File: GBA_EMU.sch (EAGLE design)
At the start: 98 parts, among them J1 USB-MINIB-5PIN, J2 AVR_SPI, SW1 LEFT, SW2 RIGHT, SW3 PWR_SWITCH, U1 MIC7221, U2 MCP1642B-ADJ, U4 LM4875, U5 Mic5365-2.8Y, U7 AZV321, X2 HEADPHONE

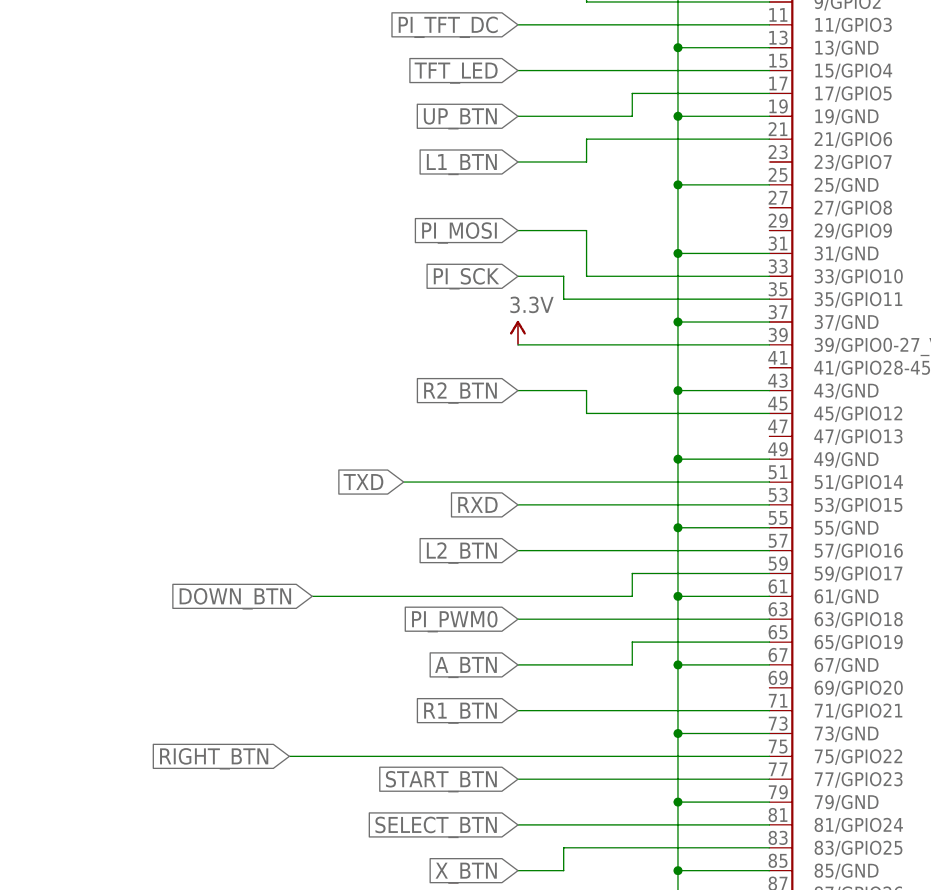
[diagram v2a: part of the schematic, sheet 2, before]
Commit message: moved connectors and whatnot
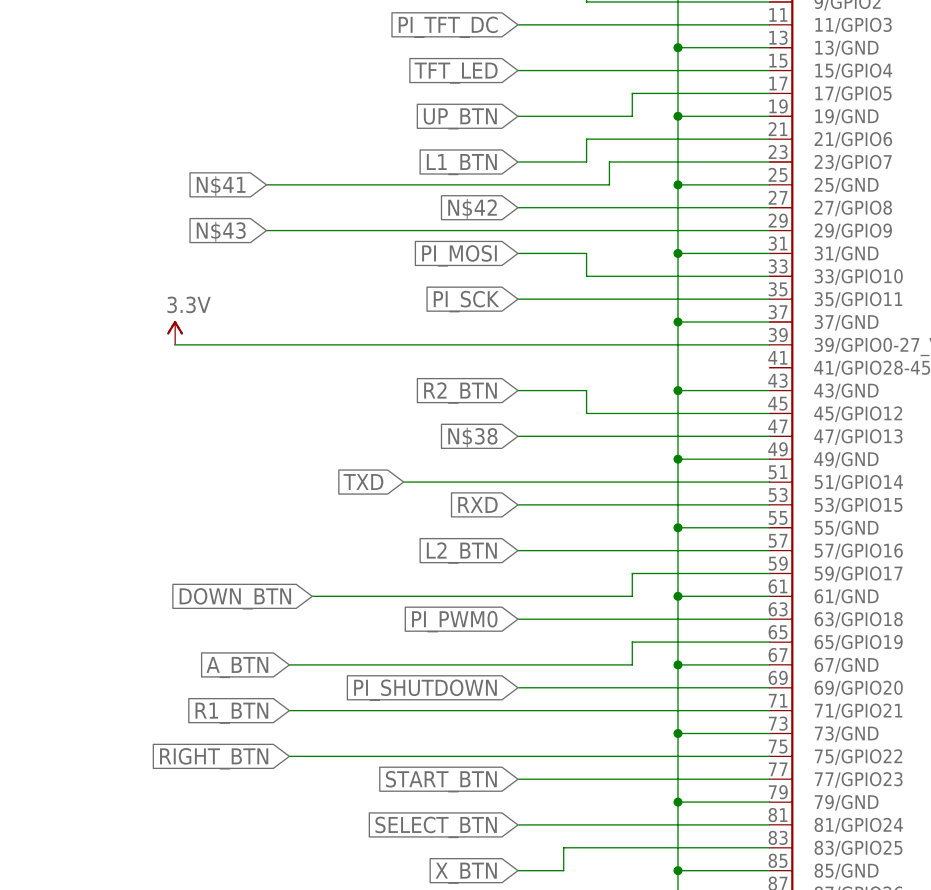
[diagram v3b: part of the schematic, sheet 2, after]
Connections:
- new net N$38: PCB1.47/GPIO13
- new net N$41: PCB1.23/GPIO7
- new net N$42: PCB1.27/GPIO8
- new net N$43: PCB1.29/GPIO9
- new net PI_SHUTDOWN: PCB1.69/GPIO20
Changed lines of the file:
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@@
 <instance part="FRAME2" gate="G$1" x="-106.68" y="-104.14"/>
 <instance part="FRAME2" gate="G$2" x="223.52" y="-104.14"/>
-<instance part="SUPPLY5" gate="G$1" x="10.16" y="106.68"/>
+<instance part="SUPPLY5" gate="G$1" x="-27.94" y="106.68"/>
 <instance part="SUPPLY11" gate="G$1" x="167.64" y="165.1"/>
 <instance part="GND13" gate="1" x="167.64" y="137.16"/>
@@
 <pinref part="SUPPLY5" gate="G$1" pin="3.3V"/>
 <pinref part="PCB1" gate="G$1" pin="39/GPIO0-27_VREF"/>
-<wire x1="10.16" y1="106.68" x2="38.1" y2="106.68" width="0.1524" layer="91"/>
+<wire x1="-27.94" y1="106.68" x2="38.1" y2="106.68" width="0.1524" layer="91"/>
 </segment>
 <segment>
@@
 <wire x1="38.1" y1="73.66" x2="22.86" y2="73.66" width="0.1524" layer="91"/>
 <wire x1="22.86" y1="73.66" x2="22.86" y2="71.12" width="0.1524" layer="91"/>
-<wire x1="22.86" y1="71.12" x2="10.16" y2="71.12" width="0.1524" layer="91"/>
-<label x="10.16" y="71.12" size="1.778" layer="95" rot="R180" xref="yes"/>
+<wire x1="22.86" y1="71.12" x2="-15.24" y2="71.12" width="0.1524" layer="91"/>
+<label x="-15.24" y="71.12" size="1.778" layer="95" rot="R180" xref="yes"/>
 </segment>
 </net>
@@
 <pinref part="PCB1" gate="G$1" pin="33/GPIO10"/>
 <wire x1="38.1" y1="114.3" x2="17.78" y2="114.3" width="0.1524" layer="91"/>
-<wire x1="17.78" y1="114.3" x2="17.78" y2="119.38" width="0.1524" layer="91"/>
-<wire x1="17.78" y1="119.38" x2="10.16" y2="119.38" width="0.1524" layer="91"/>
-<label x="10.16" y="119.38" size="1.778" layer="95" rot="R180" xref="yes"/>
+<wire x1="17.78" y1="114.3" x2="17.78" y2="116.84" width="0.1524" layer="91"/>
+<wire x1="17.78" y1="116.84" x2="10.16" y2="116.84" width="0.1524" layer="91"/>
+<label x="10.16" y="116.84" size="1.778" layer="95" rot="R180" xref="yes"/>
 </segment>
 </net>
@@
 <segment>
 <pinref part="PCB1" gate="G$1" pin="35/GPIO11"/>
-<wire x1="38.1" y1="111.76" x2="15.24" y2="111.76" width="0.1524" layer="91"/>
-<wire x1="15.24" y1="111.76" x2="15.24" y2="114.3" width="0.1524" layer="91"/>
-<wire x1="15.24" y1="114.3" x2="10.16" y2="114.3" width="0.1524" layer="91"/>
-<label x="10.16" y="114.3" size="1.778" layer="95" rot="R180" xref="yes"/>
+<wire x1="38.1" y1="111.76" x2="10.16" y2="111.76" width="0.1524" layer="91"/>
+<label x="10.16" y="111.76" size="1.778" layer="95" rot="R180" xref="yes"/>
 </segment>
 </net>
@@
 <segment>
 <pinref part="PCB1" gate="G$1" pin="71/GPIO21"/>
-<wire x1="38.1" y1="66.04" x2="10.16" y2="66.04" width="0.1524" layer="91"/>
-<label x="10.16" y="66.04" size="1.778" layer="95" rot="R180" xref="yes"/>
+<wire x1="38.1" y1="66.04" x2="-15.24" y2="66.04" width="0.1524" layer="91"/>
+<label x="-15.24" y="66.04" size="1.778" layer="95" rot="R180" xref="yes"/>
 </segment>
 </net>
@@
 </segment>
 </net>
+<net name="PI_SHUTDOWN" class="0">
+<segment>
+<pinref part="PCB1" gate="G$1" pin="69/GPIO20"/>
+<wire x1="38.1" y1="68.58" x2="10.16" y2="68.58" width="0.1524" layer="91"/>
+<label x="10.16" y="68.58" size="1.778" layer="95" rot="R180" xref="yes"/>
+</segment>
+</net>
+<net name="N$38" class="0">
+<segment>
+<pinref part="PCB1" gate="G$1" pin="47/GPIO13"/>
+<wire x1="38.1" y1="96.52" x2="10.16" y2="96.52" width="0.1524" layer="91"/>
+<label x="10.16" y="96.52" size="1.778" layer="95" rot="R180" xref="yes"/>
+</segment>
+</net>
+<net name="N$41" class="0">
+<segment>
+<pinref part="PCB1" gate="G$1" pin="23/GPIO7"/>
+<wire x1="38.1" y1="127" x2="20.32" y2="127" width="0.1524" layer="91"/>
+<wire x1="20.32" y1="127" x2="20.32" y2="124.46" width="0.1524" layer="91"/>
+<wire x1="20.32" y1="124.46" x2="-17.78" y2="124.46" width="0.1524" layer="91"/>
+<label x="-17.78" y="124.46" size="1.778" layer="95" rot="R180" xref="yes"/>
+</segment>
+</net>
+<net name="N$42" class="0">
+<segment>
+<pinref part="PCB1" gate="G$1" pin="27/GPIO8"/>
+<wire x1="38.1" y1="121.92" x2="10.16" y2="121.92" width="0.1524" layer="91"/>
+<label x="10.16" y="121.92" size="1.778" layer="95" rot="R180" xref="yes"/>
+</segment>
+</net>
+<net name="N$43" class="0">
+<segment>
+<pinref part="PCB1" gate="G$1" pin="29/GPIO9"/>
+<wire x1="38.1" y1="119.38" x2="-17.78" y2="119.38" width="0.1524" layer="91"/>
+<label x="-17.78" y="119.38" size="1.778" layer="95" rot="R180" xref="yes"/>
+</segment>
+</net>

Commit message: updated board render
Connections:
- removed net N$38: PCB1.47/GPIO13
- net Y_BTN: now also PCB1.47/GPIO13
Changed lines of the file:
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@@
 </segment>
 </net>
-<net name="N$38" class="0">
+<net name="Y_BTN" class="0">
 <segment>
 <pinref part="PCB1" gate="G$1" pin="47/GPIO13"/>

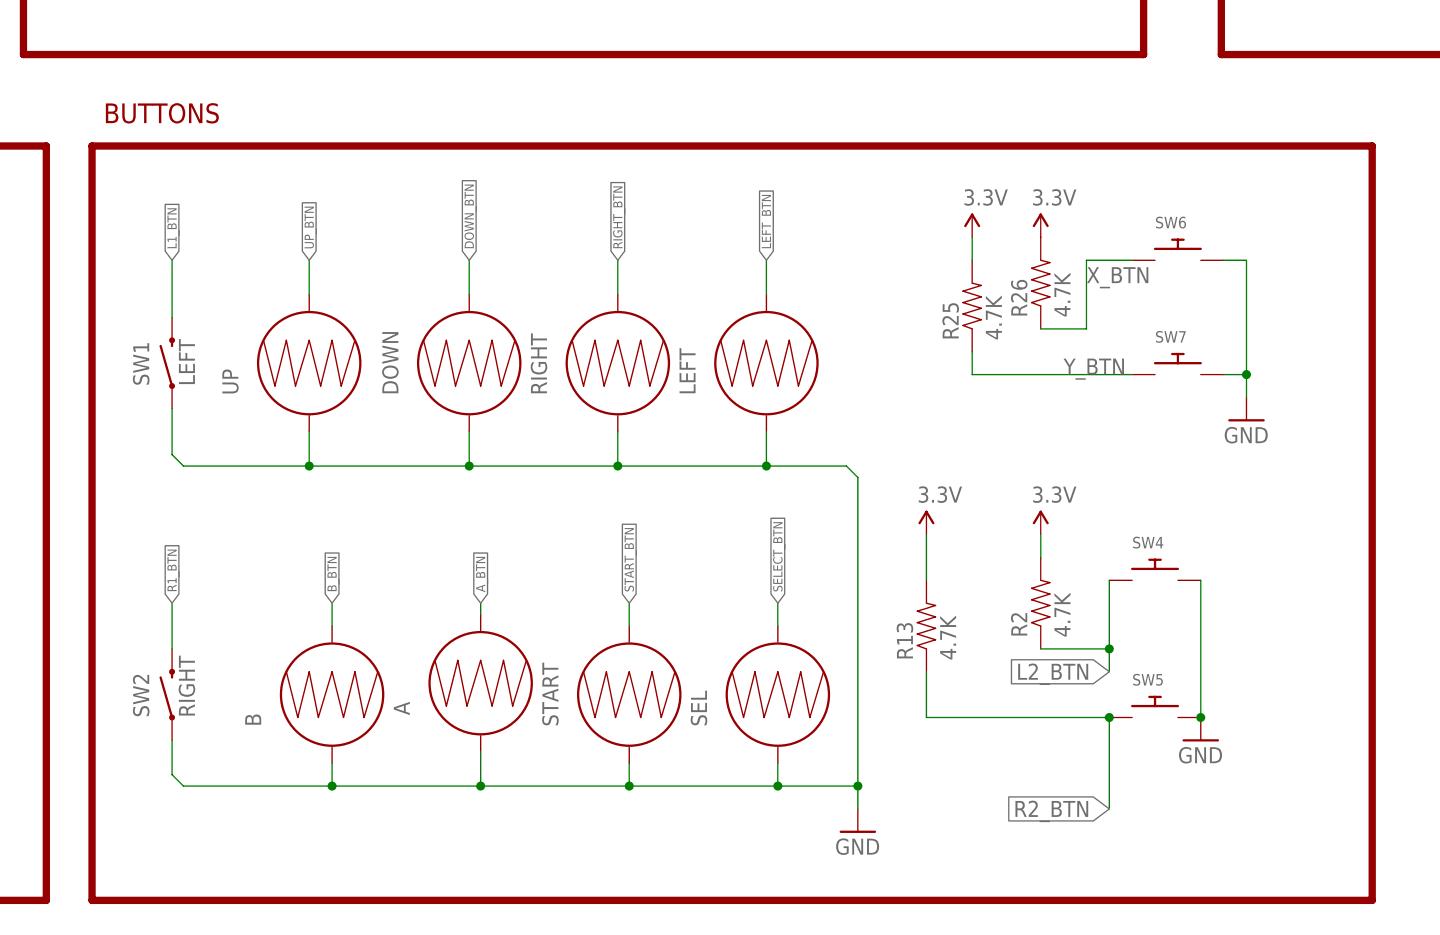
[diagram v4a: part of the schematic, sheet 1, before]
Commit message: moved some labels around
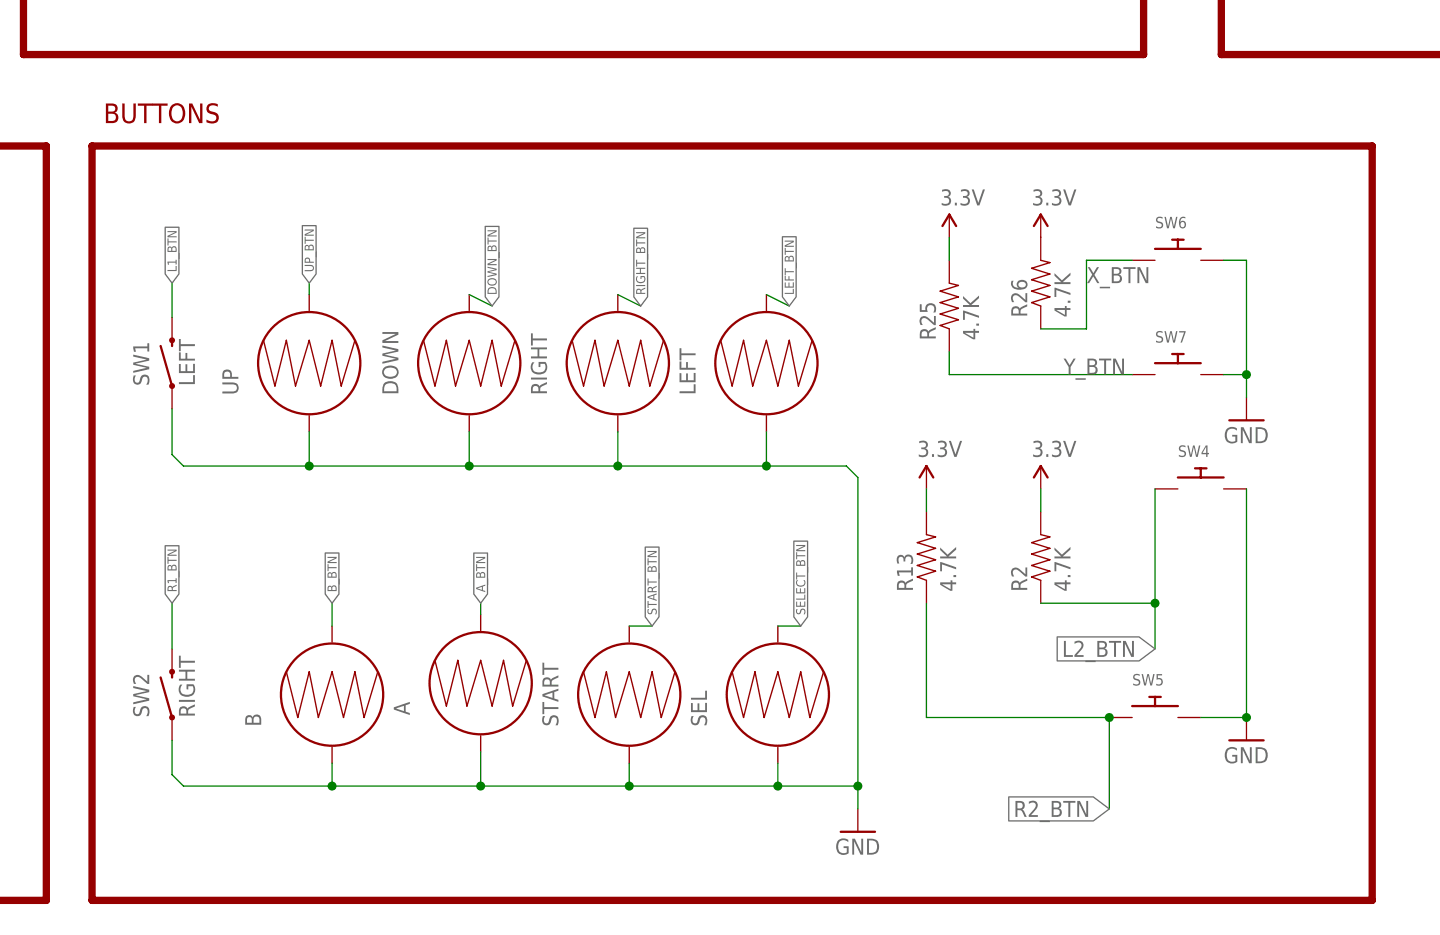
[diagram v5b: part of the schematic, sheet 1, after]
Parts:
- added R24: 10K, SparkFun-Resistors:10KOHM-1/10W-1%(0603)0603
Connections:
- new net N$38: R24.2
- net PWR_EN: now also R24.1
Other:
- moved on the sheet: R13, R2, R25, SW4
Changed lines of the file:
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@@
 <part name="SUPPLY34" library="SparkFun-Aesthetics" deviceset="3.3V" device=""/>
 <part name="SUPPLY38" library="SparkFun-Aesthetics" deviceset="1.8V" device=""/>
+<part name="R24" library="SparkFun-Resistors" deviceset="10KOHM-1/10W-1%(0603)" device="0603" value="10K"/>
 </parts>
 <sheets>
@@
 <instance part="U$1" gate="G$1" x="238.76" y="12.7"/>
 <instance part="POT1" gate="SW" x="304.8" y="152.4" rot="R90"/>
-<instance part="SW4" gate="G$1" x="426.72" y="2.54"/>
+<instance part="SW4" gate="G$1" x="431.8" y="12.7"/>
 <instance part="SW5" gate="G$1" x="426.72" y="-12.7"/>
-<instance part="GND16" gate="1" x="431.8" y="-15.24"/>
-<instance part="SUPPLY9" gate="G$1" x="401.32" y="7.62"/>
-<instance part="R13" gate="G$1" x="401.32" y="-2.54" rot="R90"/>
+<instance part="GND16" gate="1" x="436.88" y="-15.24"/>
+<instance part="SUPPLY9" gate="G$1" x="401.32" y="12.7"/>
+<instance part="R13" gate="G$1" x="401.32" y="5.08" rot="R90"/>
 <instance part="GND19" gate="1" x="436.88" y="20.32"/>
 <instance part="SW6" gate="G$1" x="429.26" y="38.1"/>
 <instance part="SW7" gate="G$1" x="429.26" y="25.4"/>
 <instance part="GND23" gate="1" x="220.98" y="-15.24"/>
-<instance part="SUPPLY35" gate="G$1" x="406.4" y="40.64"/>
+<instance part="SUPPLY35" gate="G$1" x="403.86" y="40.64"/>
 <instance part="SUPPLY36" gate="G$1" x="414.02" y="40.64"/>
-<instance part="R25" gate="G$1" x="406.4" y="33.02" rot="R90"/>
+<instance part="R25" gate="G$1" x="403.86" y="33.02" rot="R90"/>
 <instance part="R26" gate="G$1" x="414.02" y="35.56" rot="R90"/>
 <instance part="SUPPLY37" gate="G$1" x="228.6" y="193.04"/>
-<instance part="R2" gate="G$1" x="414.02" y="0" rot="R90"/>
-<instance part="SUPPLY1" gate="G$1" x="414.02" y="7.62"/>
+<instance part="R2" gate="G$1" x="414.02" y="5.08" rot="R90"/>
+<instance part="SUPPLY1" gate="G$1" x="414.02" y="12.7"/>
 <instance part="U1" gate="U$1" x="474.98" y="175.26"/>
 <instance part="R3" gate="G$1" x="477.52" y="193.04"/>
@@
 <pinref part="GND16" gate="1" pin="GND"/>
 <pinref part="SW4" gate="G$1" pin="P$2"/>
-<wire x1="431.8" y1="2.54" x2="431.8" y2="-12.7" width="0.1524" layer="91"/>
-<junction x="431.8" y="-12.7"/>
+<wire x1="436.88" y1="12.7" x2="436.88" y2="-12.7" width="0.1524" layer="91"/>
+<junction x="436.88" y="-12.7"/>
+<wire x1="436.88" y1="-12.7" x2="431.8" y2="-12.7" width="0.1524" layer="91"/>
 </segment>
 <segment>
@@
 <segment>
 <pinref part="UP" gate="S$1" pin="2"/>
-<wire x1="332.74" y1="34.29" x2="332.74" y2="38.1" width="0.1524" layer="91"/>
-<label x="332.74" y="38.1" size="1.016" layer="95" rot="R90" xref="yes"/>
+<wire x1="332.74" y1="34.29" x2="332.74" y2="35.56" width="0.1524" layer="91"/>
+<label x="332.74" y="35.56" size="1.016" layer="95" rot="R90" xref="yes"/>
 </segment>
 </net>
@@
 <segment>
 <pinref part="DOWN" gate="S$1" pin="2"/>
-<wire x1="350.52" y1="34.29" x2="350.52" y2="38.1" width="0.1524" layer="91"/>
-<label x="350.52" y="38.1" size="1.016" layer="95" rot="R90" xref="yes"/>
+<wire x1="350.52" y1="34.29" x2="353.06" y2="33.02" width="0.1524" layer="91"/>
+<label x="353.06" y="33.02" size="1.016" layer="95" rot="R90" xref="yes"/>
 </segment>
 </net>
@@
 <segment>
 <pinref part="RIGHT" gate="S$1" pin="2"/>
-<wire x1="367.03" y1="34.29" x2="367.03" y2="38.1" width="0.1524" layer="91"/>
-<label x="367.03" y="38.1" size="1.016" layer="95" rot="R90" xref="yes"/>
+<wire x1="367.03" y1="34.29" x2="369.57" y2="33.02" width="0.1524" layer="91"/>
+<label x="369.57" y="33.02" size="1.016" layer="95" rot="R90" xref="yes"/>
 </segment>
 </net>
@@
 <segment>
 <pinref part="LEFT" gate="S$1" pin="2"/>
-<wire x1="383.54" y1="34.29" x2="383.54" y2="38.1" width="0.1524" layer="91"/>
-<label x="383.54" y="38.1" size="1.016" layer="95" rot="R90" xref="yes"/>
+<wire x1="383.54" y1="34.29" x2="386.08" y2="33.02" width="0.1524" layer="91"/>
+<label x="386.08" y="33.02" size="1.016" layer="95" rot="R90" xref="yes"/>
 </segment>
 </net>
@@
 <segment>
 <pinref part="SW1" gate="SW$1" pin="2"/>
-<wire x1="317.5" y1="31.75" x2="317.5" y2="38.1" width="0.1524" layer="91"/>
-<label x="317.5" y="38.1" size="1.016" layer="95" rot="R90" xref="yes"/>
+<wire x1="317.5" y1="31.75" x2="317.5" y2="35.56" width="0.1524" layer="91"/>
+<label x="317.5" y="35.56" size="1.016" layer="95" rot="R90" xref="yes"/>
 </segment>
 </net>
@@
 <segment>
 <pinref part="START" gate="G$1" pin="2"/>
-<wire x1="368.3" y1="-2.54" x2="368.3" y2="0" width="0.1524" layer="91"/>
-<label x="368.3" y="0" size="1.016" layer="95" rot="R90" xref="yes"/>
+<wire x1="368.3" y1="-2.54" x2="370.84" y2="-2.54" width="0.1524" layer="91"/>
+<label x="370.84" y="-2.54" size="1.016" layer="95" rot="R90" xref="yes"/>
 </segment>
 </net>
@@
 <segment>
 <pinref part="SEL" gate="G$1" pin="2"/>
-<wire x1="384.81" y1="-2.54" x2="384.81" y2="0" width="0.1524" layer="91"/>
-<label x="384.81" y="0" size="1.016" layer="95" rot="R90" xref="yes"/>
+<wire x1="384.81" y1="-2.54" x2="387.35" y2="-2.54" width="0.1524" layer="91"/>
+<label x="387.35" y="-2.54" size="1.016" layer="95" rot="R90" xref="yes"/>
 </segment>
 </net>
@@
 <pinref part="SUPPLY9" gate="G$1" pin="3.3V"/>
 <pinref part="R13" gate="G$1" pin="2"/>
-<wire x1="401.32" y1="2.54" x2="401.32" y2="7.62" width="0.1524" layer="91"/>
+<wire x1="401.32" y1="10.16" x2="401.32" y2="12.7" width="0.1524" layer="91"/>
 </segment>
 <segment>
 <pinref part="SUPPLY35" gate="G$1" pin="3.3V"/>
 <pinref part="R25" gate="G$1" pin="2"/>
-<wire x1="406.4" y1="40.64" x2="406.4" y2="38.1" width="0.1524" layer="91"/>
+<wire x1="403.86" y1="40.64" x2="403.86" y2="38.1" width="0.1524" layer="91"/>
 </segment>
 <segment>
@@
 <pinref part="SUPPLY1" gate="G$1" pin="3.3V"/>
 <pinref part="R2" gate="G$1" pin="2"/>
-<wire x1="414.02" y1="7.62" x2="414.02" y2="5.08" width="0.1524" layer="91"/>
+<wire x1="414.02" y1="12.7" x2="414.02" y2="10.16" width="0.1524" layer="91"/>
 </segment>
 <segment>
@@
 <segment>
 <pinref part="R25" gate="G$1" pin="1"/>
-<wire x1="406.4" y1="27.94" x2="406.4" y2="25.4" width="0.1524" layer="91"/>
+<wire x1="403.86" y1="27.94" x2="403.86" y2="25.4" width="0.1524" layer="91"/>
 <pinref part="SW7" gate="G$1" pin="P$1"/>
-<wire x1="406.4" y1="25.4" x2="424.18" y2="25.4" width="0.1524" layer="91"/>
+<wire x1="403.86" y1="25.4" x2="424.18" y2="25.4" width="0.1524" layer="91"/>
 <label x="416.56" y="25.4" size="1.778" layer="95"/>
 </segment>
@@
 <segment>
 <pinref part="R2" gate="G$1" pin="1"/>
-<wire x1="414.02" y1="-5.08" x2="421.64" y2="-5.08" width="0.1524" layer="91"/>
+<wire x1="414.02" y1="0" x2="426.72" y2="0" width="0.1524" layer="91"/>
 <pinref part="SW4" gate="G$1" pin="P$1"/>
-<wire x1="421.64" y1="2.54" x2="421.64" y2="-5.08" width="0.1524" layer="91"/>
-<wire x1="421.64" y1="-5.08" x2="421.64" y2="-7.62" width="0.1524" layer="91"/>
-<junction x="421.64" y="-5.08"/>
-<label x="421.64" y="-7.62" size="1.778" layer="95" rot="R180" xref="yes"/>
+<wire x1="426.72" y1="12.7" x2="426.72" y2="0" width="0.1524" layer="91"/>
+<wire x1="426.72" y1="0" x2="426.72" y2="-5.08" width="0.1524" layer="91"/>
+<junction x="426.72" y="0"/>
+<label x="426.72" y="-5.08" size="1.778" layer="95" rot="R180" xref="yes"/>
 </segment>
 </net>
@@
 <segment>
 <pinref part="R13" gate="G$1" pin="1"/>
-<wire x1="401.32" y1="-7.62" x2="401.32" y2="-12.7" width="0.1524" layer="91"/>
+<wire x1="401.32" y1="0" x2="401.32" y2="-12.7" width="0.1524" layer="91"/>
 <pinref part="SW5" gate="G$1" pin="P$1"/>
 <wire x1="401.32" y1="-12.7" x2="421.64" y2="-12.7" width="0.1524" layer="91"/>
@@
 <instance part="GND38" gate="1" x="205.74" y="129.54"/>
 <instance part="SUPPLY38" gate="G$1" x="68.58" y="30.48"/>
+<instance part="R24" gate="G$1" x="119.38" y="162.56"/>
 </instances>
 <busses>
@@
 <wire x1="104.14" y1="139.7" x2="106.68" y2="139.7" width="0.1524" layer="91"/>
 <wire x1="106.68" y1="139.7" x2="106.68" y2="162.56" width="0.1524" layer="91"/>
-<wire x1="106.68" y1="162.56" x2="119.38" y2="162.56" width="0.1524" layer="91"/>
-<label x="119.38" y="162.56" size="1.778" layer="95" xref="yes"/>
-</segment>
-</net>
+<wire x1="106.68" y1="162.56" x2="114.3" y2="162.56" width="0.1524" layer="91"/>
+<label x="129.54" y="162.56" size="1.778" layer="95" xref="yes"/>
+<pinref part="R24" gate="G$1" pin="1"/>
+</segment>
+</net>
+<net name="N$38" class="0">
+<segment>
+<pinref part="R24" gate="G$1" pin="2"/>
+<wire x1="129.54" y1="162.56" x2="124.46" y2="162.56" width="0.1524" layer="91"/>
+</segment>
+</net>
